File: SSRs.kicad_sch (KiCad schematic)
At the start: 25 parts, among them Q1 CJ2310, Q2 CJ2310, Q3 CJ2310, Q4 CJ2310, Q5 CJ2310, Q6 CJ2310, U5 AQY212SX

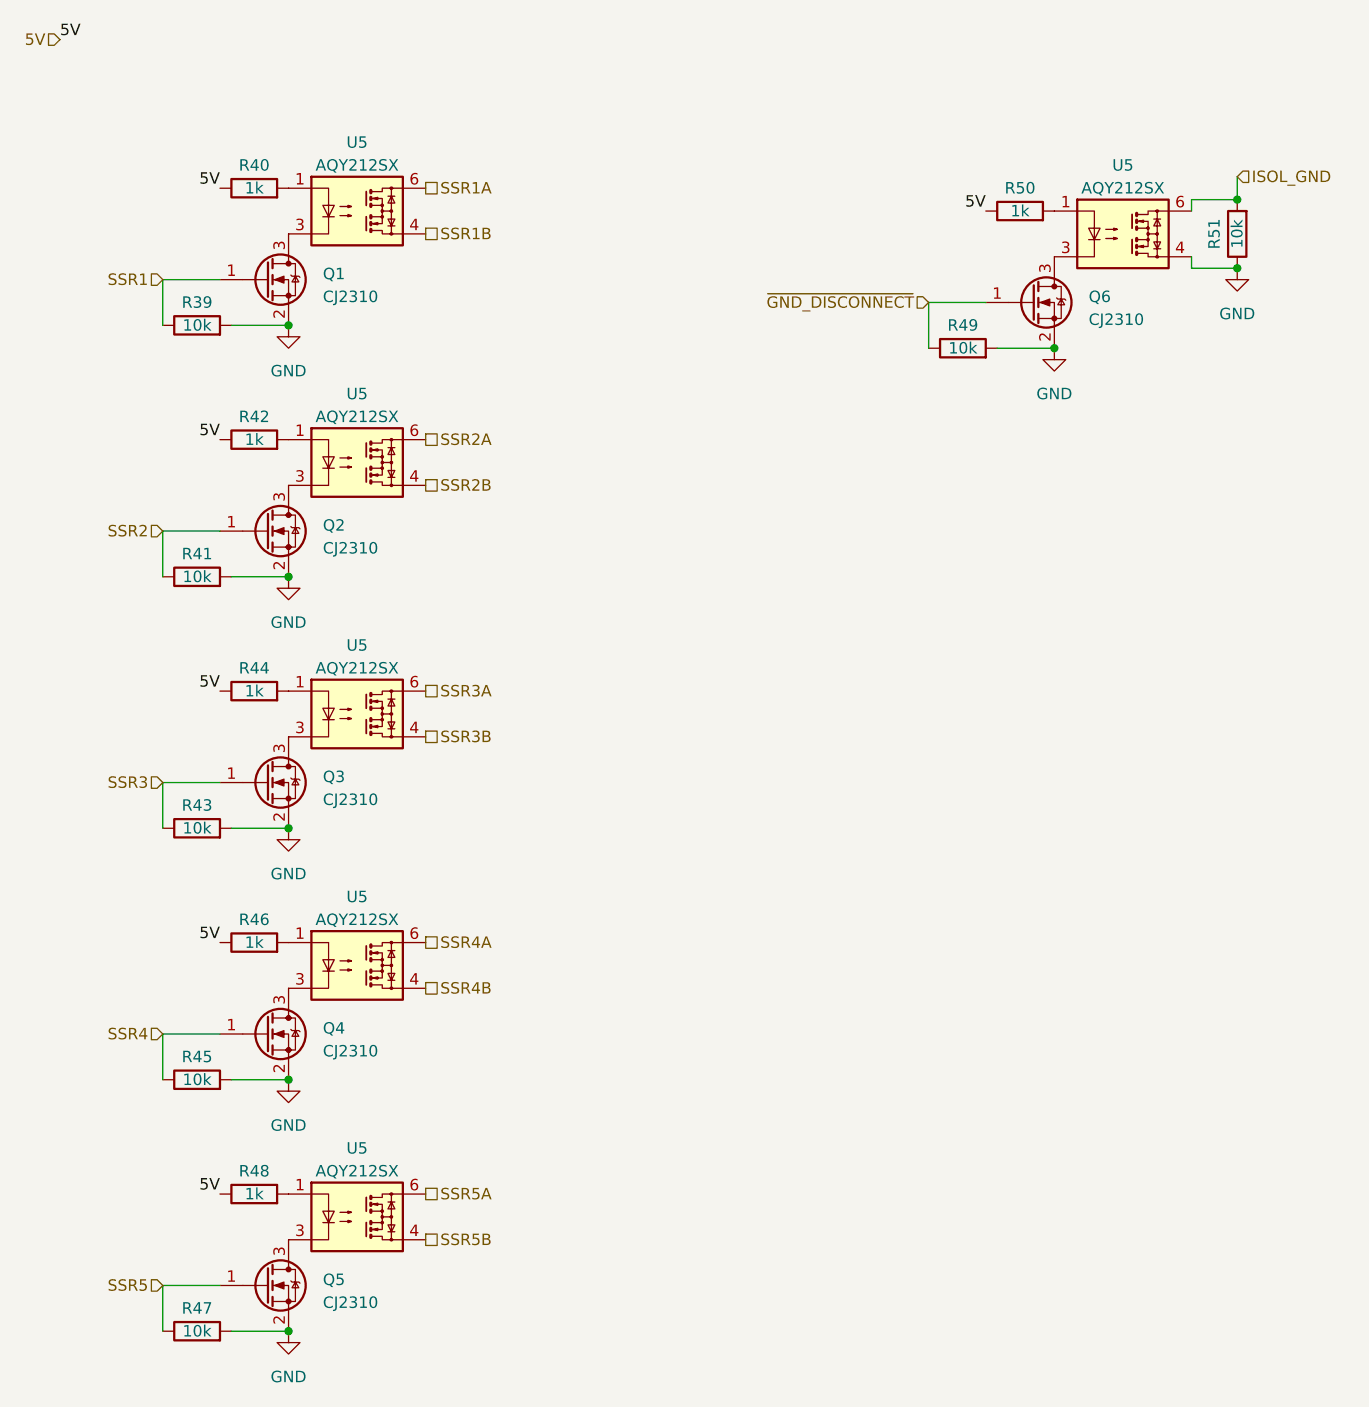
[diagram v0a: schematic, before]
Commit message: Build pogoplayground v1.0 - Fix continuity tester reference voltage - Fix SSR 5V supply
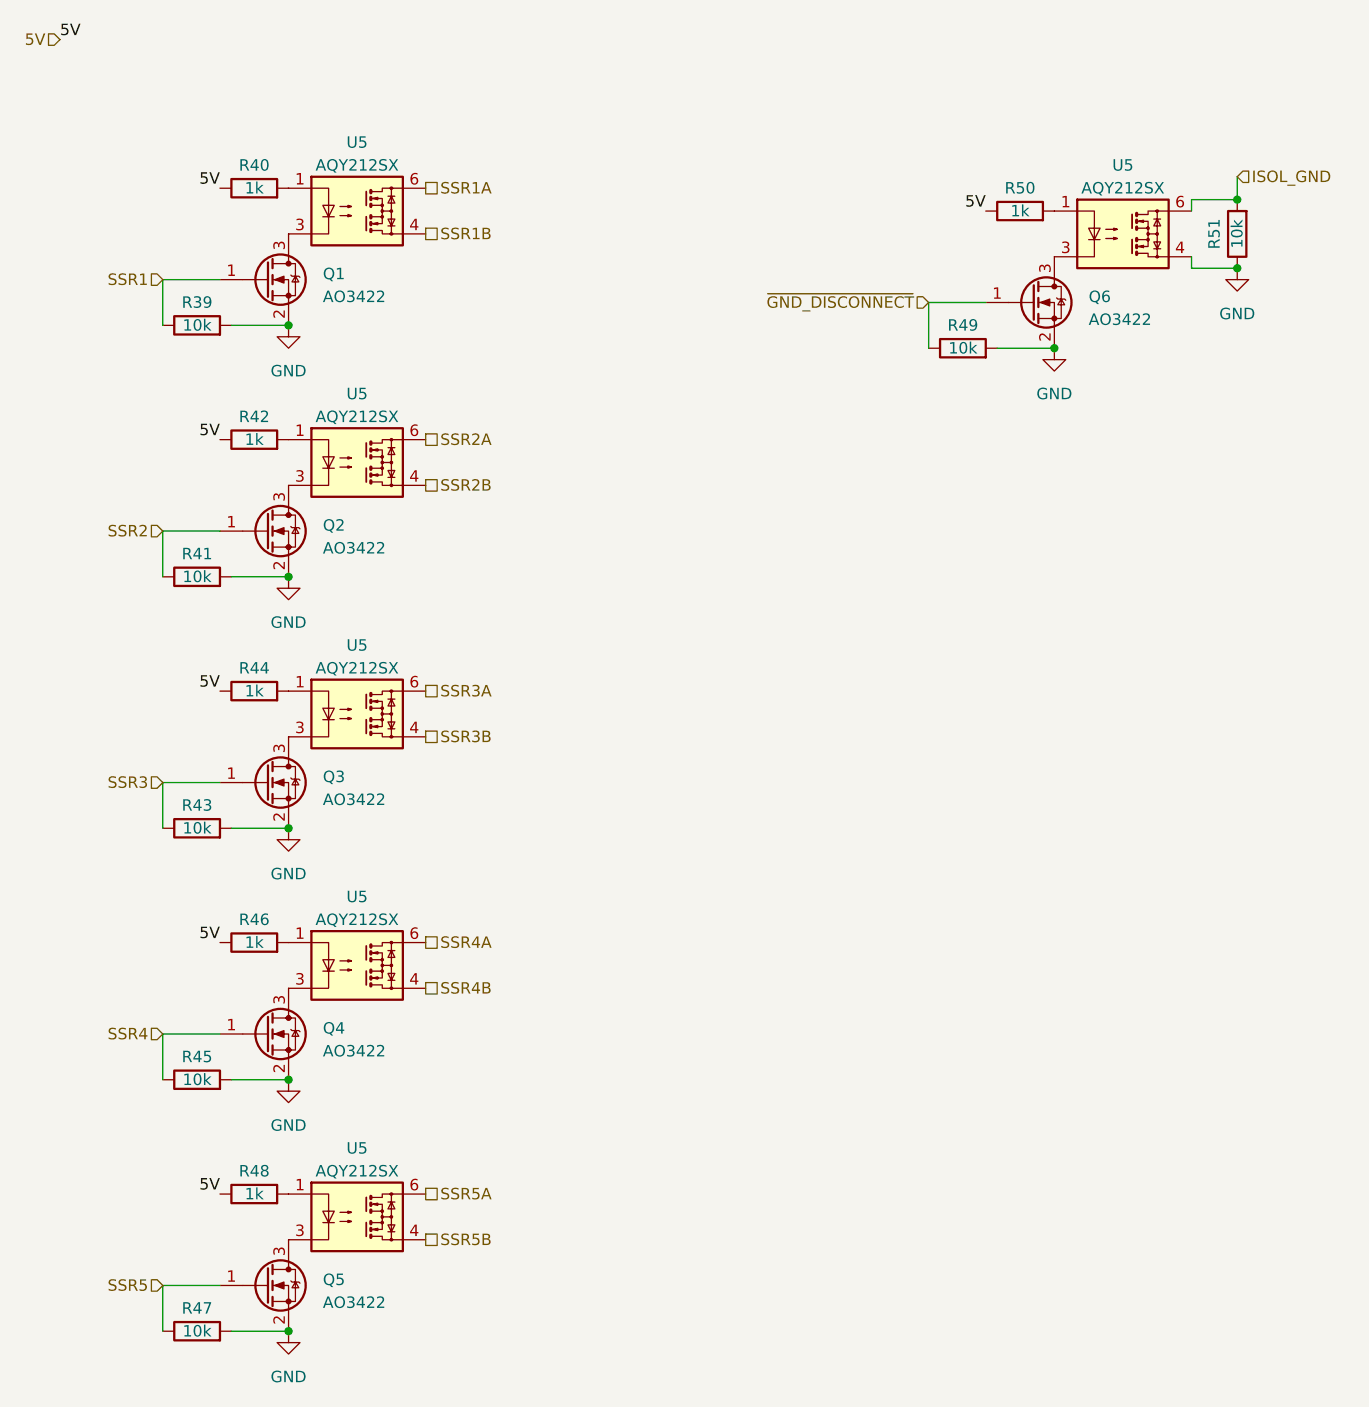
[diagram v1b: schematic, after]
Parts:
- Q1, Q2, Q3, Q4, Q5, Q6: value CJ2310 -> AO3422
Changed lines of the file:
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@@
       (effects (font (size 1.27 1.27)) (justify left))
     )
-    (property "Value" "CJ2310" (at 167.64 61.595 0)
+    (property "Value" "AO3422" (at 167.64 61.595 0)
       (effects (font (size 1.27 1.27)) (justify left))
     )
@@
       (effects (font (size 1.27 1.27)) (justify left))
     )
-    (property "Value" "CJ2310" (at 82.55 114.935 0)
+    (property "Value" "AO3422" (at 82.55 114.935 0)
       (effects (font (size 1.27 1.27)) (justify left))
     )
@@
       (effects (font (size 1.27 1.27)) (justify left))
     )
-    (property "Value" "CJ2310" (at 82.55 170.815 0)
+    (property "Value" "AO3422" (at 82.55 170.815 0)
       (effects (font (size 1.27 1.27)) (justify left))
     )
@@
       (effects (font (size 1.27 1.27)) (justify left))
     )
-    (property "Value" "CJ2310" (at 82.55 86.995 0)
+    (property "Value" "AO3422" (at 82.55 86.995 0)
       (effects (font (size 1.27 1.27)) (justify left))
     )
@@
       (effects (font (size 1.27 1.27)) (justify left))
     )
-    (property "Value" "CJ2310" (at 82.55 142.875 0)
+    (property "Value" "AO3422" (at 82.55 142.875 0)
       (effects (font (size 1.27 1.27)) (justify left))
     )
@@
       (effects (font (size 1.27 1.27)) (justify left))
     )
-    (property "Value" "CJ2310" (at 82.55 59.055 0)
-      (effects (font (size 1.27 1.27)) (justify left))
-    )
+    (property "Value" "AO3422" (at 82.55 59.055 0)
+      (effects (font (size 1.27 1.27)) (justify left))
+    )
